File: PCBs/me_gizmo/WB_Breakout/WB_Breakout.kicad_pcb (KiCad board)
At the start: 2 copper layers, 19.7 x 54.4 mm, 35 parts, among them J1 Conn_01x08_Pin, J2 Conn_01x05_Pin, J4 Conn_01x10_Pin, U1 ADG714, U2 ADG714, U3 ADG714, U4 ADG714

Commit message: Updated resistor values in schematic, moved vias off pads, added bypass capacitors
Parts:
- removed OlinLogoTruncated: G***, Eclectronics:OlinLogoTruncated
- added C1: 0.1u, Capacitor_SMD:C_0603_1608Metric, F.Cu at (149.5, 73.7)
- added C2: 0.1u, Capacitor_SMD:C_0603_1608Metric, F.Cu at (150.3, 90.6)
- added C3: 0.1u, Capacitor_SMD:C_0603_1608Metric, F.Cu at (151.0, 105.7)
- added C4: 0.1u, Capacitor_SMD:C_0603_1608Metric, F.Cu at (146.0, 120.1)
- R1, R2, R3: value R -> 10k
- R19, R20, R21, R22, R35, R36, R37, R38, R39, R40, R41, R42: value 120 -> 118
- R23, R24, R25, R26, R27, R28, R29, R30, R31, R32, R33, R34: value 350 -> 348
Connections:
- net /CIPO renamed /COPI
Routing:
- net GND: track 31.1 -> 39.6 mm, vias 18 -> 22
- net /VDD: track 81.5 -> 85.3 mm, vias 4 -> 5
- net /COPI: track 9.37 -> 11.1 mm
- net /HB_OUT1+: track 44.4 -> 45.6 mm
- net /HB_OUT2+: track 46.9 -> 48.1 mm
- net /HB_OUT1-: track 47.6 -> 48.4 mm
- net Net-(U2-DOUT): track 28.5 -> 29.1 mm
- net /SCLK: track 52.3 -> 52.8 mm
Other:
- board text added: "COPI"
- board text added: "R25"
- board text removed: "${REFERENCE}"
- board text removed: "CIPO"

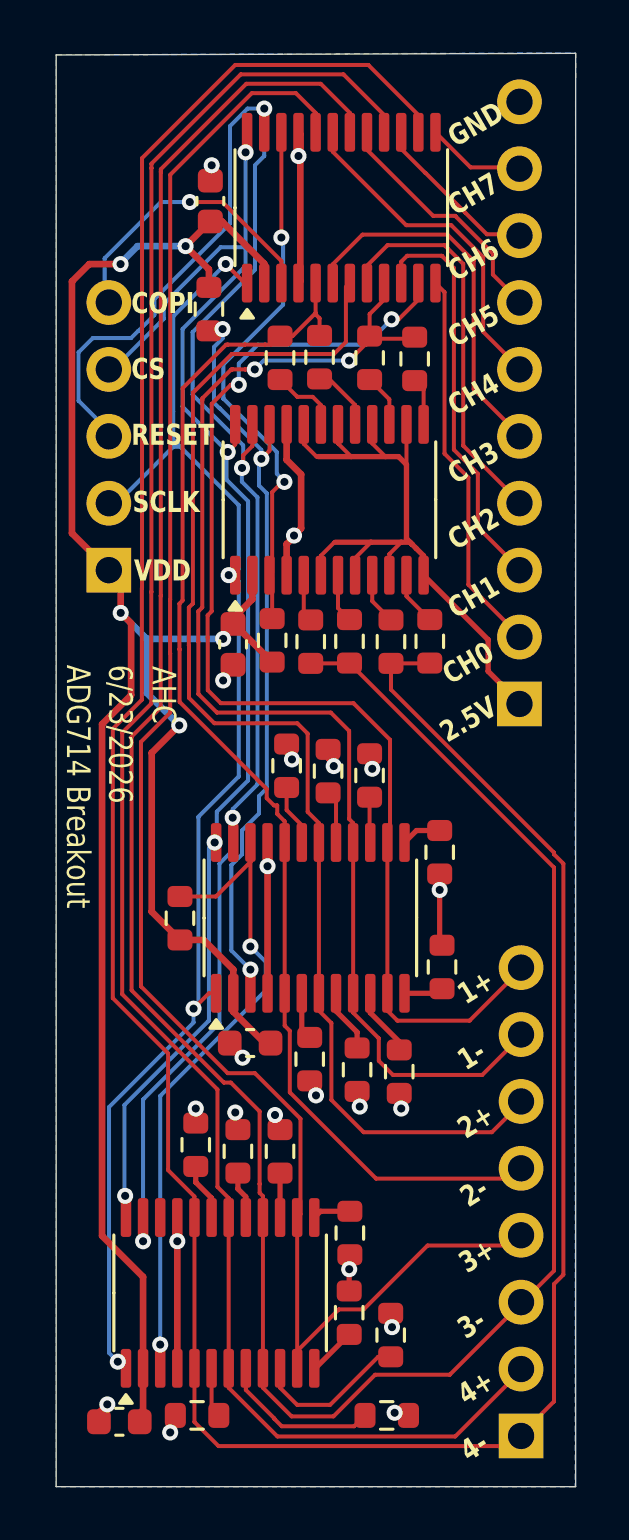
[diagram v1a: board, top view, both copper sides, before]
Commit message: Fixed pin header width in WB breakout
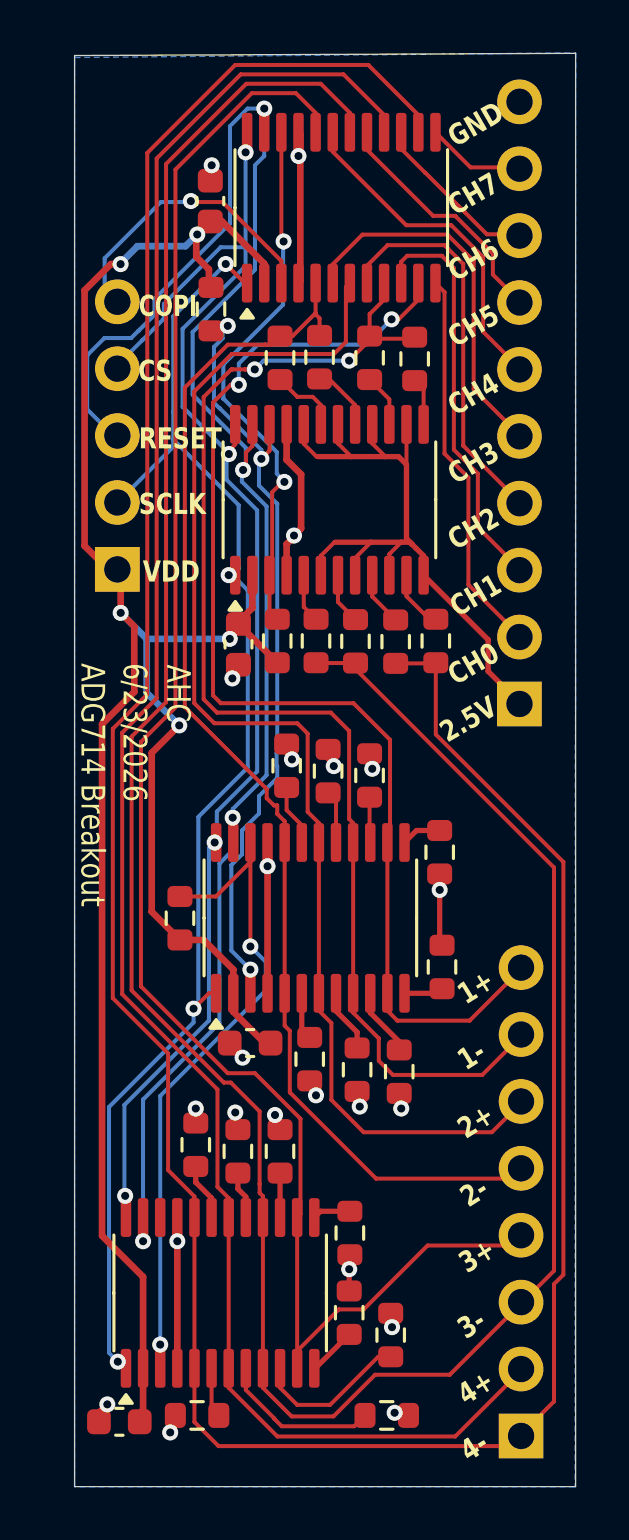
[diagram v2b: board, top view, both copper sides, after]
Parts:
- moved J2 0.32 mm to (145.9, 87.7)
- moved R26 0.23 mm to (158.0, 90.4)
- moved R23 0.23 mm to (155.0, 90.5)
- moved R19 0.20 mm to (153.5, 90.4)
- moved C2 0.20 mm to (150.5, 90.6)
- moved R3 0.20 mm to (152.0, 90.4)
- moved R22 0.18 mm to (156.5, 90.5)
- moved R1 0.08 mm to (149.5, 77.9)
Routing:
- net /HB_OUT4-: track 110.2 -> 109.4 mm
- net Net-(U2-DOUT): track 29.1 -> 29.8 mm
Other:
- board size 19.7 x 54.4 mm -> 19 x 54.4 mm
